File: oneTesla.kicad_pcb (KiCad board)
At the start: 2 copper layers, 100 x 100 mm, 44 parts, among them IC1 74HCT14, IC2 74HCT74, IC3 UCC37321P, IC4 UCC37321P, IC6 MC7805BDTRKG, J1 2EDGRC-5.08-02P, J110 Jumper 110V, P1 PRIMARIO A, P2 PRIMARIO B, Q1 FGA60N65SMD, Q2 FGA60N65SMD, T1 1:1:1, T3 1:300

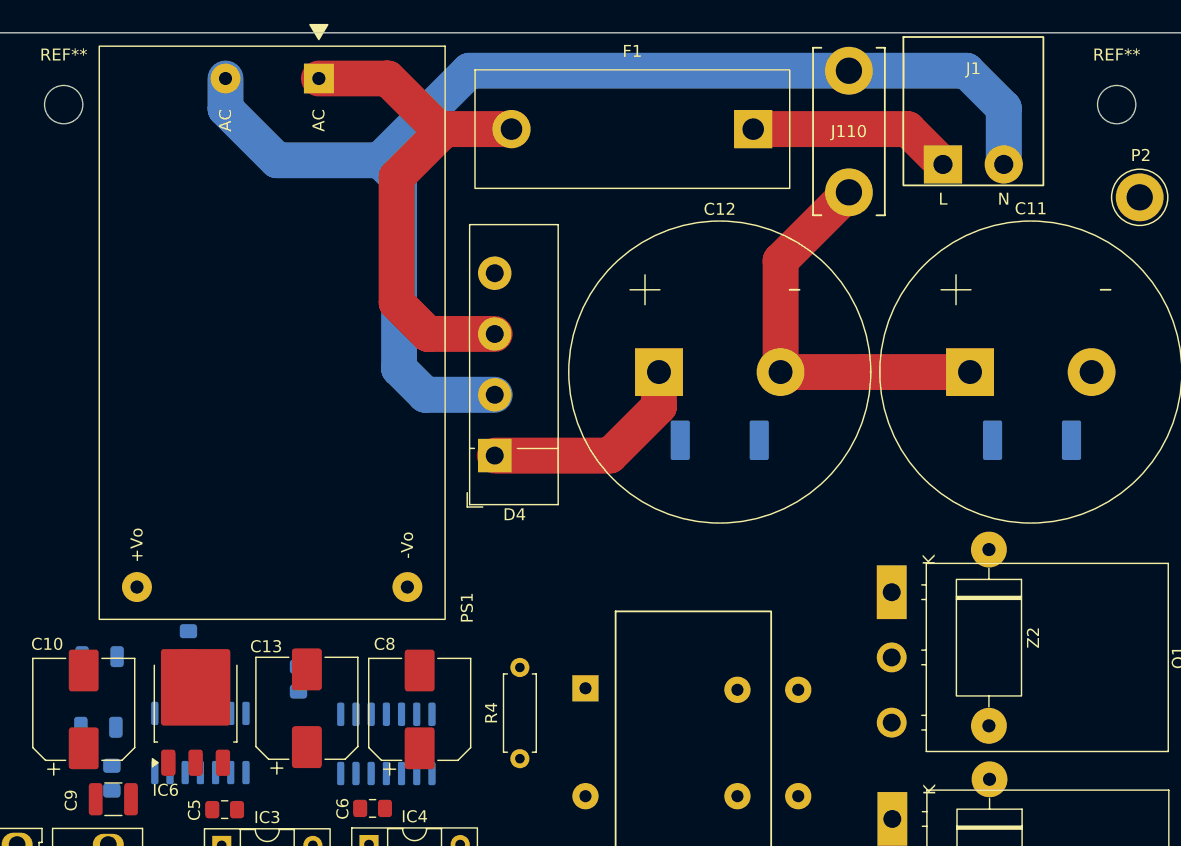
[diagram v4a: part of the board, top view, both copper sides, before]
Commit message: cad: amplia jumper 110V e configura regras de fabricacao
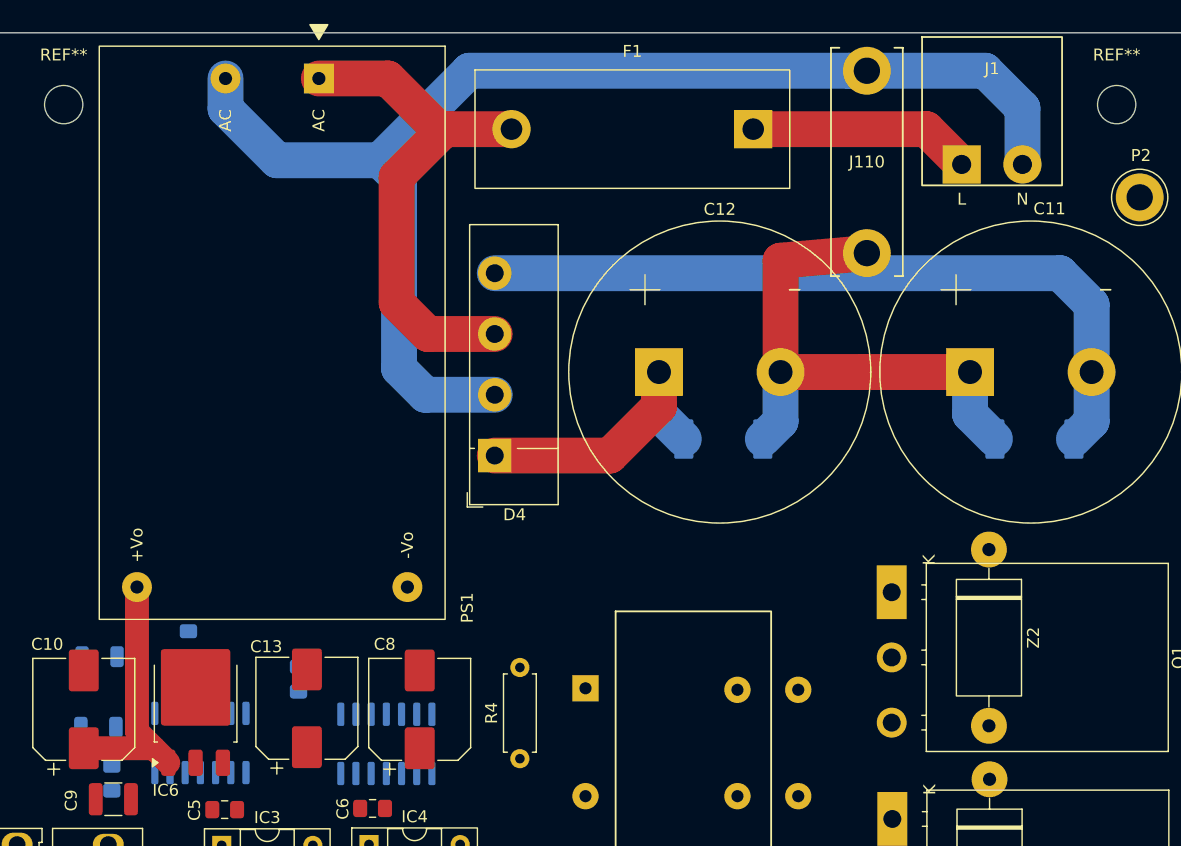
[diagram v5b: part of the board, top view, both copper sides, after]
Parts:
- J110: footprint oneTesla:J110_WireLink_P10.16mm -> oneTesla:J110_WireLink_P15.24mm
- moved R6 26.3 mm to (118.5, 61.0)
- moved R5 25.8 mm to (92.5, 61.0)
- moved J110 2.95 mm to (104.5, 37.8)
- moved J1 1.56 mm to (112.4, 38.0)
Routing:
- net /DC_MINUS: track 0.00 -> 62.8 mm
- net +15V: track 0.00 -> 21.6 mm
- net /DC_MID: track 33.4 -> 45.3 mm
- net /DC_PLUS: track 18.3 -> 24.8 mm
- net /AC_L: track 17.1 -> 18.6 mm
- net /AC_N: track 105.4 -> 107.0 mm

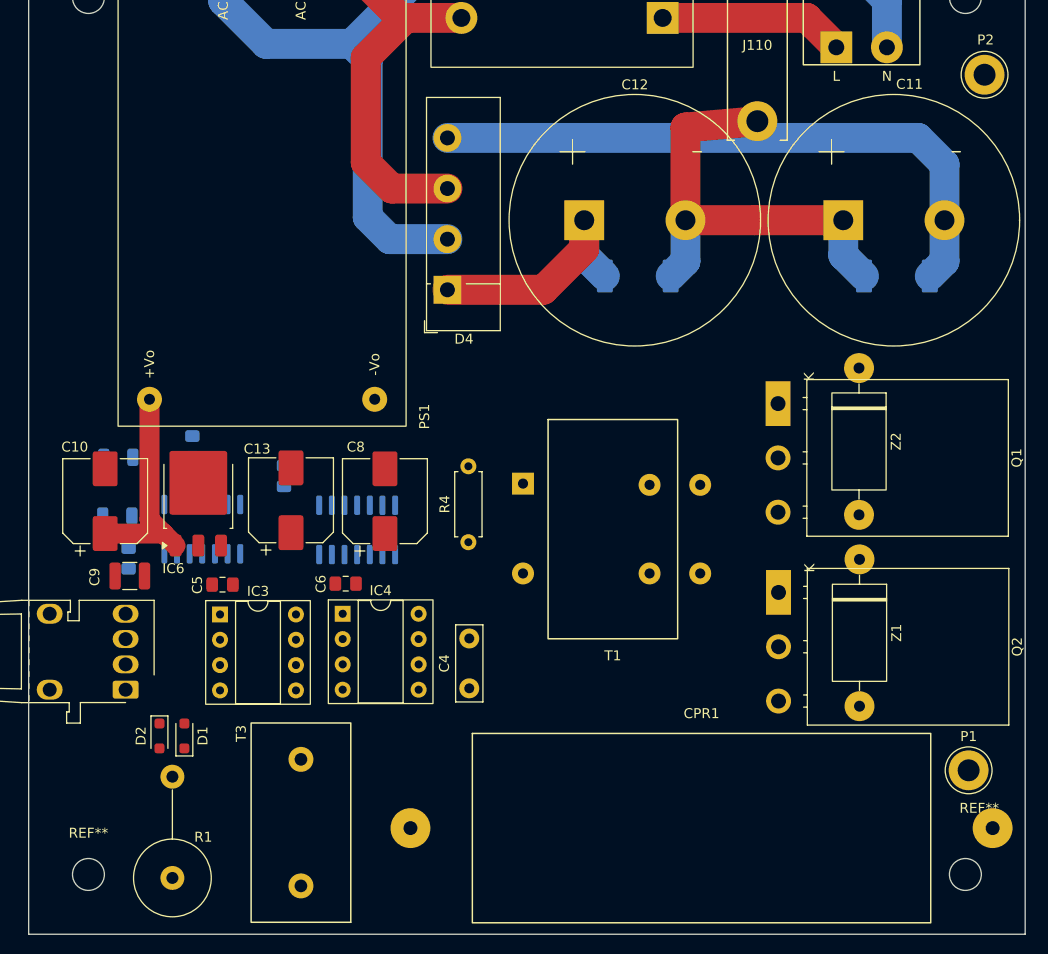
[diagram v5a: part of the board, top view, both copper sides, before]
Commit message: cad: reforca trilhas do driver IC3 e registra revisao do roteamento
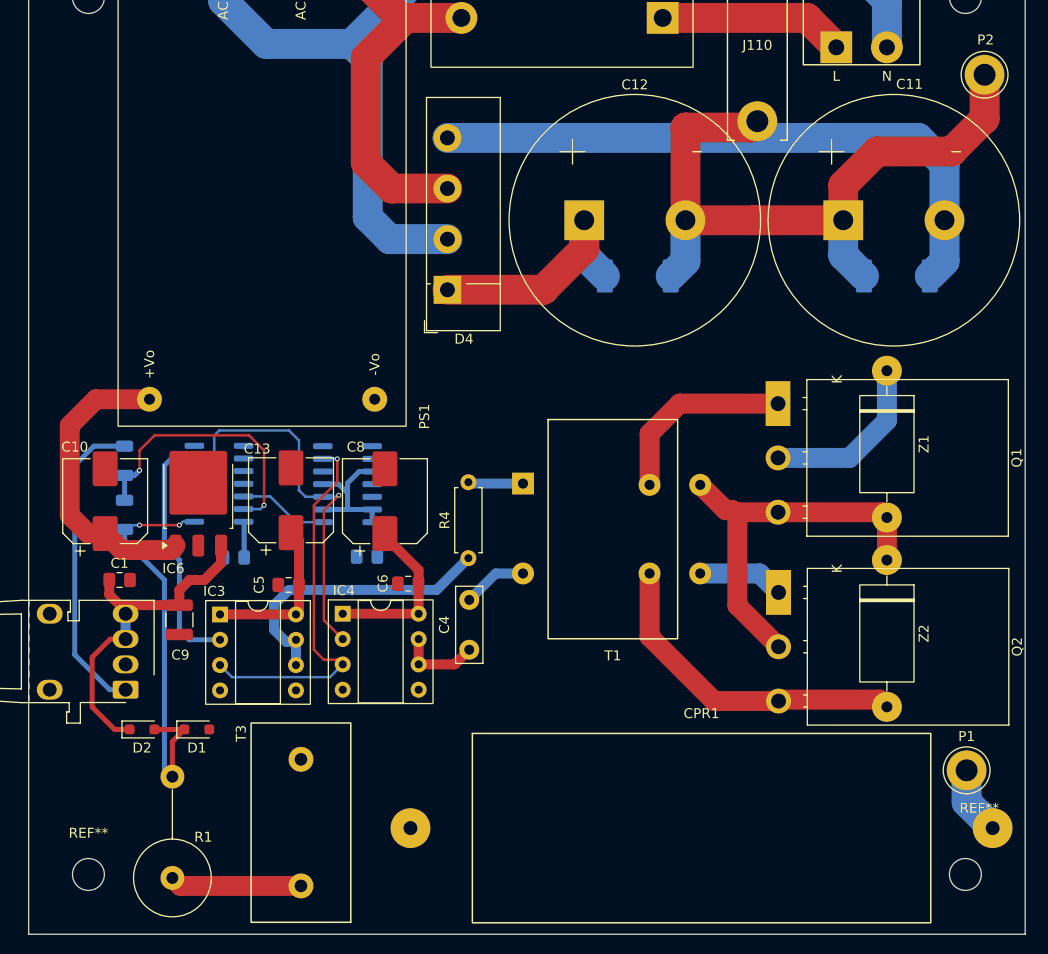
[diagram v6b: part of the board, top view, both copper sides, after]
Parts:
- C1: moved to F.Cu
- moved Z2 19.5 mm to (117.5, 96.9)
- moved Z1 19.1 mm to (117.5, 77.9)
- moved C3 11.9 mm to (52.0, 89.2), turned to 180 degrees
- moved C2 11.6 mm to (65.3, 89.2), turned to 180 degrees
- moved C9 6.64 mm to (46.5, 95.5), turned to -90 degrees
- moved C5 6.64 mm to (57.5, 92.0), turned to 180 degrees
- moved C6 6.27 mm to (69.5, 91.9), turned to 180 degrees
- moved R3 5.81 mm to (41.0, 85.0), turned to 90 degrees
- moved R2 5.59 mm to (41.0, 79.5), turned to -90 degrees
- moved IC1 4.85 mm to (50.5, 81.8), turned to 0 degrees
- moved IC2 4.69 mm to (63.4, 81.9), turned to 0 degrees
- moved C4 3.87 mm to (75.6, 98.5)
- moved C1 2.34 mm to (40.5, 91.5), turned to 0 degrees
- moved D2 1.87 mm to (42.8, 106.5), turned to 0 degrees
- moved R4 1.60 mm to (75.5, 89.3)
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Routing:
- net +5V: track 0.00 -> 56.9 mm
- net Net-(D1-K): track 0.00 -> 42.4 mm, vias 0 -> 2
- net +15V: track 21.6 -> 63.7 mm
- net Net-(IC2A-C): track 0.00 -> 40.8 mm, vias 0 -> 1
- net /SW_NODE: track 0.00 -> 39.6 mm
- net /DRIVE_ENABLE: track 0.00 -> 38.4 mm, vias 0 -> 1
- net /DC_MINUS: track 62.8 -> 96.0 mm
- net /OPTICAL_OUT: track 0.00 -> 31.4 mm
- net Net-(IC3-OUT-Pad6): track 0.00 -> 29.3 mm
- net Net-(IC1-Pad13): track 0.00 -> 27.7 mm, vias 0 -> 2
- net /DC_MID: track 45.3 -> 70.4 mm
- net Net-(IC3-IN): track 0.00 -> 24.9 mm
- net /GATE_H: track 0.00 -> 19.3 mm
- net /DC_PLUS: track 24.8 -> 42.2 mm
- net Net-(T3-S1): track 0.00 -> 13.2 mm
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
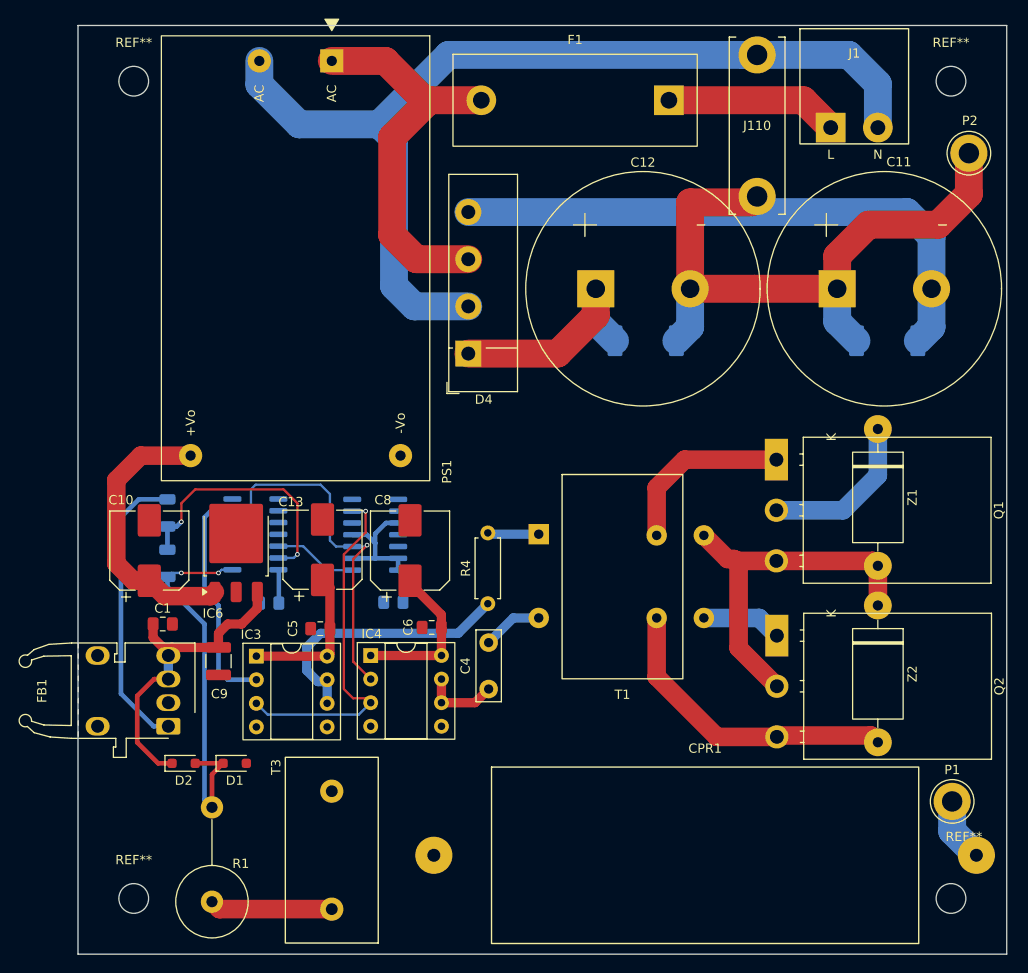
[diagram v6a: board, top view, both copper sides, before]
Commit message: feat: finalize ARCSTRIKE rev 1.2 PCB updates
Refine copper zones, restore the T3 primary wire jumper, correct FB1 pads and silkscreen, and add plated fuseholder slots. Include validation reports, previews, and revision backups.
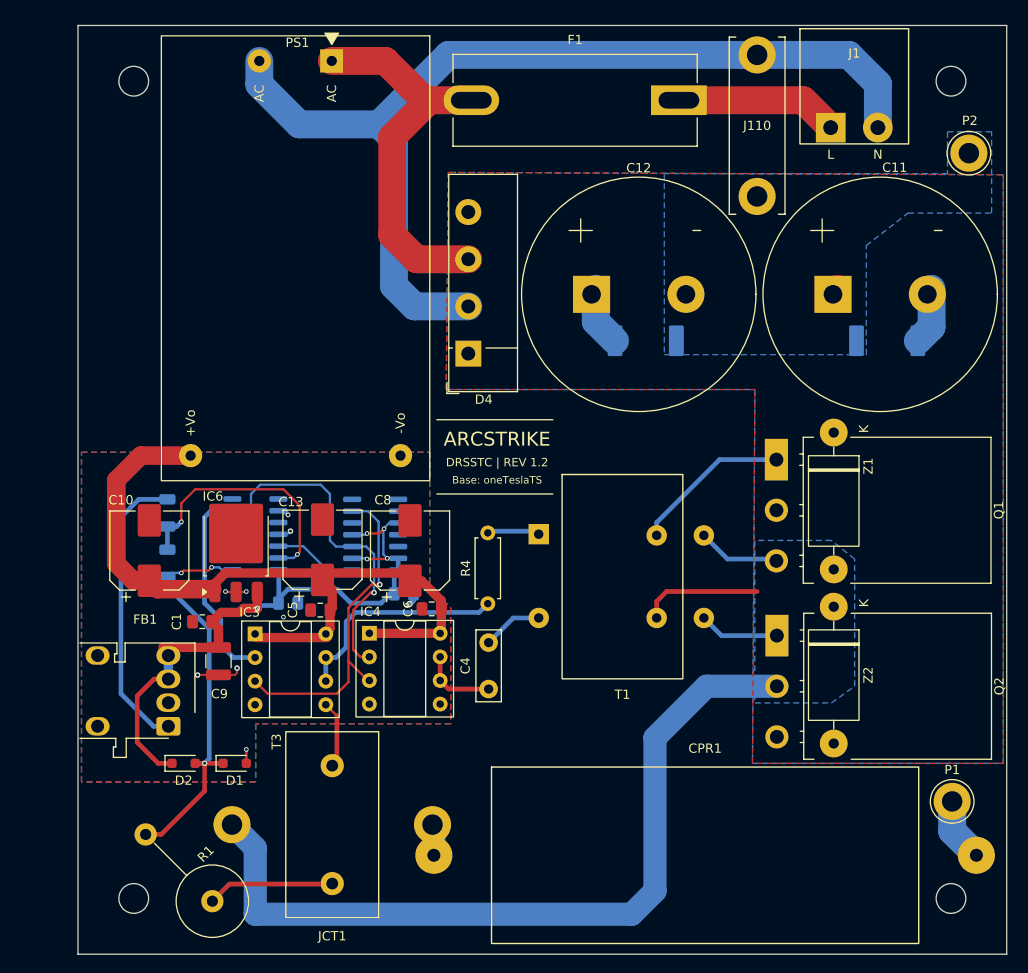
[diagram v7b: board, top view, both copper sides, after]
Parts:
- added JCT1: FIO PELO T3, oneTesla:CT_Primary_WireLink_P21.59mm, F.Cu at (58.8, 113.1)
- F1: footprint oneTesla:Fuseholder_Idall_AS-06_5x20mm_P20.20mm_Horizontal -> oneTesla:Fuseholder_Idall_AS-06_5x20mm_Slotted_P22.35mm
- moved Z1 4.77 mm to (112.8, 78.2)
- moved Z2 4.75 mm to (112.8, 97.0)
- moved C1 4.26 mm to (44.8, 91.2), turned to 180 degrees
- moved R1 3.83 mm to (42.2, 117.8), turned to 135 degrees
- moved T3 2.75 mm to (58.8, 113.1)
- moved IC3 2.39 mm to (50.4, 92.6)
- moved IC4 2.39 mm to (62.8, 92.5)
- moved C3 2.04 mm to (54.0, 89.2), turned to 0 degrees
- moved C5 2.00 mm to (57.5, 90.0)
- moved C6 2.00 mm to (69.5, 89.9)
- moved C2 1.45 mm to (66.5, 88.2), turned to 0 degrees
- moved C11 0.75 mm to (117.8, 56.0)
- moved C12 0.75 mm to (91.8, 56.0)
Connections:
- CPR1 pad 1: /SW_NODE -> /SW_CT
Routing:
- net /DC_MINUS: track 96.0 -> 19.5 mm
- net /DC_MID: track 70.4 -> 0.21 mm
- net /SW_NODE: track 39.6 -> 95.6 mm
- net /DC_PLUS: track 42.2 -> 6.46 mm
- net GND: track 0.00 -> 20.8 mm, vias 0 -> 9
- net +15V: track 63.7 -> 81.8 mm
- net +5V: track 56.9 -> 72.2 mm, vias 0 -> 5
- net Net-(IC3-OUT-Pad6): track 29.3 -> 24.3 mm
- net /SW_CT: track 0.00 -> 3.36 mm
- net Net-(IC3-IN): track 24.9 -> 22.0 mm
- net Net-(D1-K): track 42.4 -> 44.9 mm, vias 2 -> 3
- net /GATE_H: track 19.3 -> 17.1 mm
- net /DRIVE_ENABLE: track 38.4 -> 36.8 mm
- net Net-(IC2A-C): track 40.8 -> 39.3 mm
- added copper zone on B.Cu, net /DC_MID
- added copper zone on F.Cu, net /DC_MINUS
- added copper zone on B.Cu, net /DC_PLUS
- added copper zone on B.Cu, net /SW_NODE
- added copper zone on B.Cu, net GND
- added copper zone on F.Cu, net GND
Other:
- board text added: "ARCSTRIKE"
- board text added: "Base: oneTeslaTS"
- board text added: "DRSSTC | REV 1.2"

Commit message: chore: save latest PCB routing and silkscreen edits
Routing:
- net /SW_NODE: track 95.6 -> 94.3 mm
- net /GATE_H: track 17.1 -> 18.3 mm
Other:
- board text added: "DRSSTC | REV 0.1"
- board text added: "TESLACOIL"
- board text added: "by: Uriel Contardi"
- board text removed: "ARCSTRIKE"
- board text removed: "Base: oneTeslaTS"
- board text removed: "DRSSTC | REV 1.2"
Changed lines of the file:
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@@
 	)
 	(gr_line
-		(start 70 69.5)
-		(end 82.5 69.5)
-		(stroke
-			(width 0.12)
-			(type solid)
-		)
-		(layer "F.SilkS")
-	)
-	(gr_line
-		(start 70 77.5)
-		(end 82.5 77.5)
+		(start 33.15 67.5)
+		(end 33.15 55)
 		(stroke
 			(width 0.12)
@@
 		)
 	)
-	(gr_text "Base: oneTeslaTS"
-		(at 76.5 76 0)
+	(gr_text "by: Uriel Contardi\n"
+		(at 37.75 46 90)
 		(layer "F.SilkS")
 		(effects
 			(font
-				(size 0.8 0.8)
-				(thickness 0.12)
+				(size 0.9 0.9)
+				(thickness 0.15)
 			)
 		)
 	)
-	(gr_text "DRSSTC | REV 1.2"
-		(at 76.5 74.1 0)
+	(gr_text "DRSSTC | REV 0.1"
+		(at 37.75 61 90)
 		(layer "F.SilkS")
 		(effects
@@
 		)
 	)
-	(gr_text "ARCSTRIKE"
-		(at 76.5 71.6 0)
+	(gr_text "TESLACOIL"
+		(at 35.25 61 90)
 		(layer "F.SilkS")
 		(effects
@@
 	)
 	(segment
-		(start 100.668 92.75)
-		(end 106.625 92.75)
-		(width 0.5)
-		(layer "B.Cu")
-		(net "/GATE_L")
-	)
-	(segment
 		(start 98.763 90.845)
 		(end 100.668 92.75)
 		(width 0.5)
-		(layer "B.Cu")
+		(layer "F.Cu")
 		(net "/GATE_L")
 	)
 	(segment
-		(start 93.5 103.75)
-		(end 93.5 120.25)
-		(width 2.5)
-		(layer "B.Cu")
-		(net "/SW_NODE")
+		(start 100.668 92.75)
+		(end 106.625 92.75)
+		(width 0.5)
+		(layer "F.Cu")
+		(net "/GATE_L")
 	)
 	(segment
-		(start 50.455 122.75)
-		(end 50.455 115.6)
+		(start 50.455 115.6)
+		(end 47.955 113.1)
 		(width 2.5)
 		(layer "B.Cu")
@@
 	)
 	(segment
-		(start 93.5 120.25)
-		(end 91 122.75)
+		(start 89.75 124)
+		(end 55.75 124)
 		(width 2.5)
 		(layer "B.Cu")
@@
 	)
 	(segment
-		(start 50.455 115.6)
-		(end 47.955 113.1)
+		(start 50.455 118.705)
+		(end 50.455 115.6)
 		(width 2.5)
 		(layer "B.Cu")
@@
 	)
 	(segment
-		(start 91 122.75)
-		(end 50.455 122.75)
+		(start 93.5 103.75)
+		(end 93.5 120.25)
+		(width 2.5)
+		(layer "B.Cu")
+		(net "/SW_NODE")
+	)
+	(segment
+		(start 93.5 120.25)
+		(end 89.75 124)
 		(width 2.5)
 		(layer "B.Cu")
@@
 	)
 	(segment
+		(start 55.75 124)
+		(end 50.455 118.705)
+		(width 2.5)
+		(layer "B.Cu")
+		(net "/SW_NODE")
+	)
+	(segment
 		(start 106.775 103.5)
 		(end 106.625 103.65)
@@
 	)
 	(segment
-		(start 100.45 73.8)
+		(start 98.45 73.8)
 		(end 106.575 73.8)
 		(width 0.5)
-		(layer "B.Cu")
+		(layer "F.Cu")
 		(net "/GATE_H")
 	)
 	(segment
-		(start 93.683 81.955)
-		(end 93.683 80.567)
+		(start 93.683 78.567)
+		(end 98.45 73.8)
 		(width 0.5)
-		(layer "B.Cu")
+		(layer "F.Cu")
 		(net "/GATE_H")
 	)
 	(segment
-		(start 93.683 80.567)
-		(end 100.45 73.8)
+		(start 93.683 81.955)
+		(end 93.683 78.567)
 		(width 0.5)
-		(layer "B.Cu")
+		(layer "F.Cu")
 		(net "/GATE_H")
 	)
